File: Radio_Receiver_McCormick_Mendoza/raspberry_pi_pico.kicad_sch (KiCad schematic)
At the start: 9 parts, among them J27 Conn_01x20_Socket, J28 Conn_01x01_Pin, J29 Conn_01x20_Socket, U4 Pico

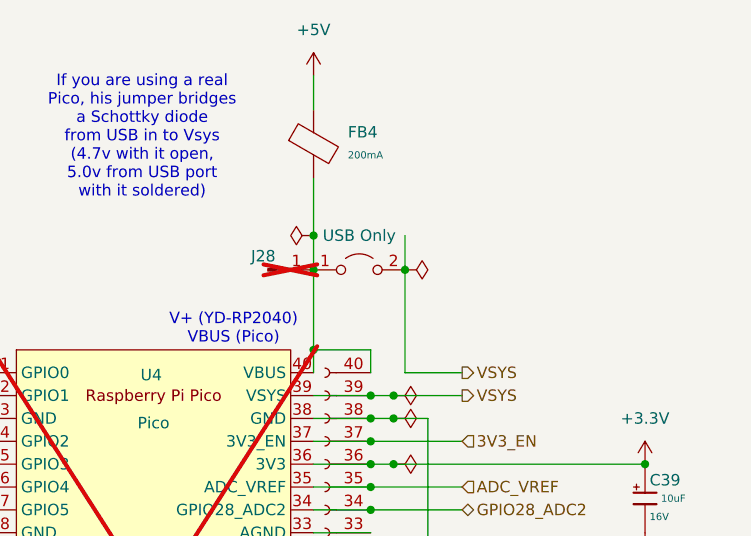
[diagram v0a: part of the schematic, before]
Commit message: Added bibliography source and schematic edits
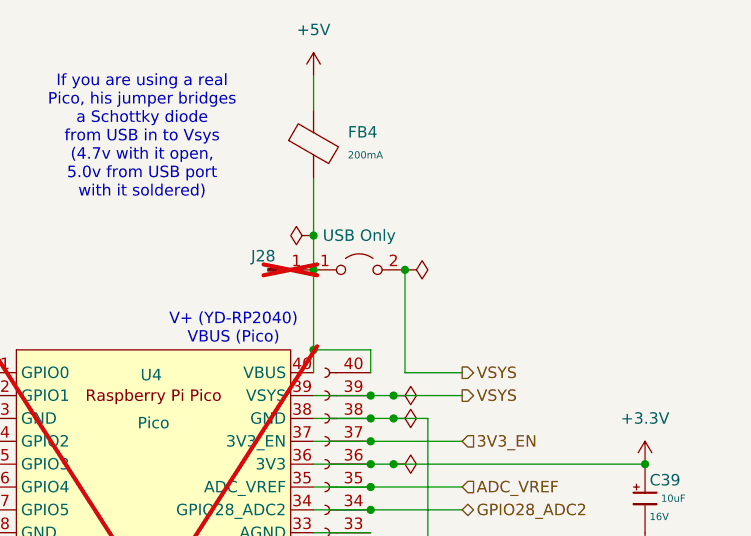
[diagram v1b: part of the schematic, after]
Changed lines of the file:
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@@
-	(wire
-		(pts
-			(xy 167.64 48.26) (xy 167.64 52.07)
-		)
-		(stroke
-			(width 0)
-			(type default)
-		)
-	)
 	(wire
 		(pts
@@
 		(length 2.54)
 		(shape round)
-		(at 172.72 73.66 90)
+		(at 189.23 73.66 180)
 		(fields_autoplaced yes)
 		(effects
@@
 				(size 1.27 1.27)
 			)
-			(justify left bottom)
+			(justify right bottom)
 		)
 		(property "Net Class" "1V1"
-			(at 170.18 72.9615 90)
+			(at 189.9285 76.2 0)
 			(hide yes)
 			(show_name no)
@@
 		)
 		(property "Component Class" ""
-			(at -41.91 5.08 0)
+			(at -25.4 5.08 0)
 			(hide yes)
 			(show_name no)

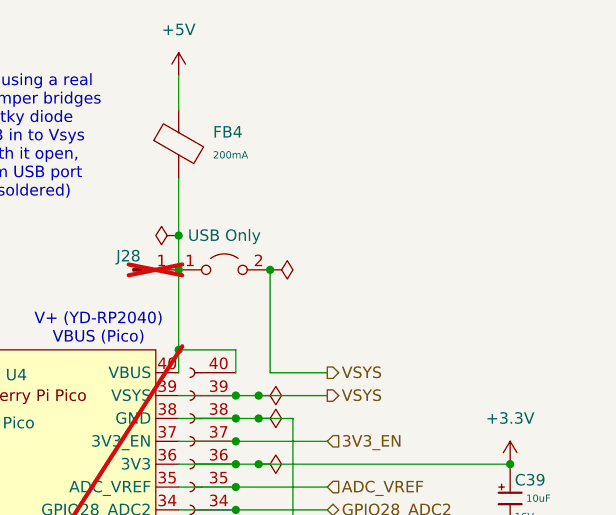
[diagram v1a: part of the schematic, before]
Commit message: Added reference voltage stability by buffer amp
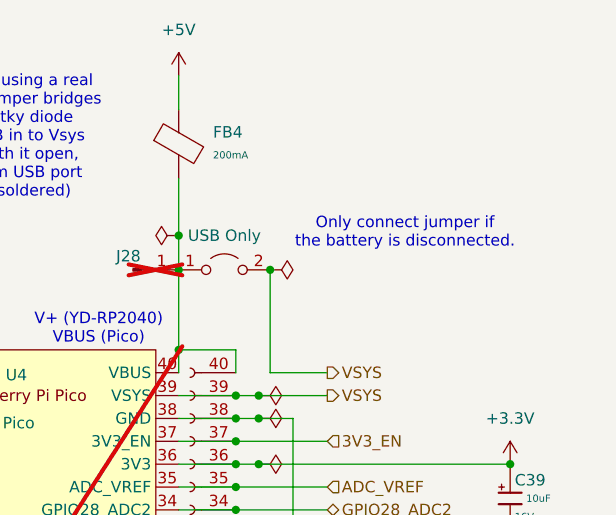
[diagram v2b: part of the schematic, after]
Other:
- note added: "Only connect jumper if the battery is disconnected."
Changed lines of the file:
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@@
 		(comment 3 "Jeffrey McCormick")
+	)
+	(text "Only connect jumper if\nthe battery is disconnected."
+		(exclude_from_sim no)
+		(at 182.626 48.006 0)
+		(effects
+			(font
+				(size 1.27 1.27)
+			)
+		)
 	)
 	(text "V+ (YD-RP2040)\nVBUS (Pico)"

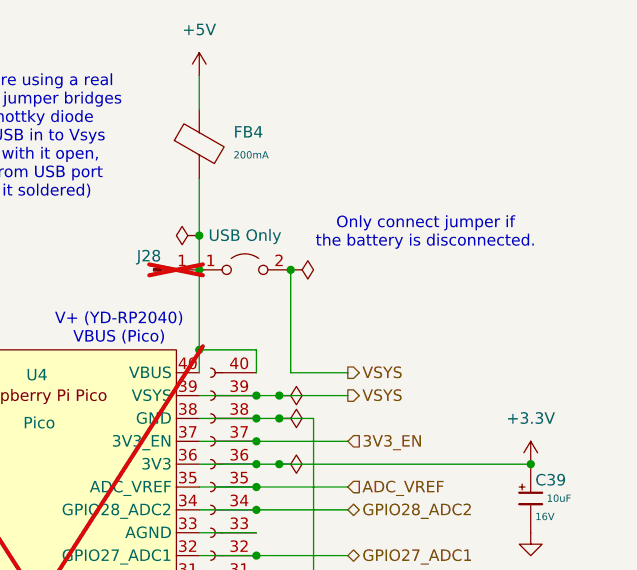
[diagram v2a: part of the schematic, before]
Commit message: Added digital power regulator
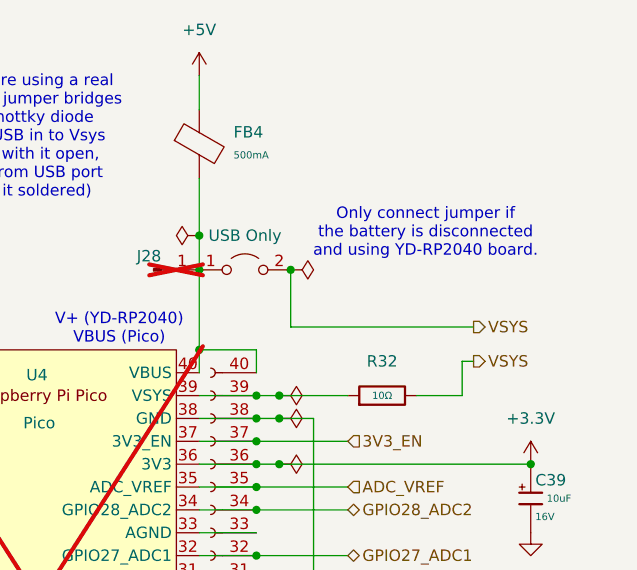
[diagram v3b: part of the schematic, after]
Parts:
- removed FB4: (no value), PCM_JLCPCB:FB_0603, symbol PCM_JLCPCB-Inductors:Ferrite,0603
- added FB4: (no value), PCM_JLCPCB:FB_0805, symbol PCM_JLCPCB-Inductors:Ferrite,0805,(2)
- added R32: 10Ω, PCM_JLCPCB:R_0805, symbol PCM_JLCPCB-Resistors:0805,10Ω
- C39: Manufacturer AVX -> (none)
- R30: Manufacturer UNI-ROYAL(Uniroyal Elec) -> (none)
- S2: Manufacturer XUNPU -> (none)
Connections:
- net +5V: now also FB4.1
- net VSYS: now also R32.2; no longer J29.39 (Pin_2), U4.39 (VSYS)
- net at J28.1 (Pin_1), J29.40 (Pin_1), JP69.1 (A)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: now also FB4.2
- new net: J29.39 (Pin_2), R32.1, U4.39 (VSYS)
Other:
- note added: "Only connect jumper if the battery is disconnected and using YD-RP2040 board."
- note removed: "Only connect jumper if the battery is disconnected."

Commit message: Integrated signal path modules
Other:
- note added: "To Digital parts (OLED, DAC, etc.)"
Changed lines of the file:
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@@
+		)
+	)
+	(text "To Digital parts\n(OLED, DAC, etc.)"
+		(exclude_from_sim no)
+		(at 205.74 71.374 0)
+		(effects
+			(font
+				(size 1.27 1.27)
+			)
 		)
 	)

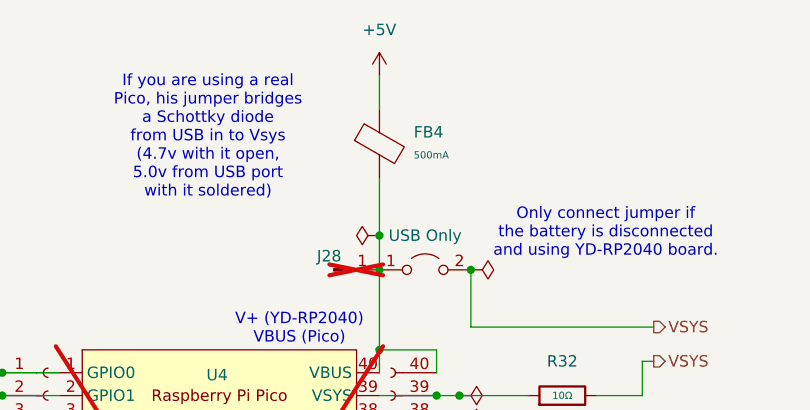
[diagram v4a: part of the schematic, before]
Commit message: Finalized Pico connections and added indicator LEDs
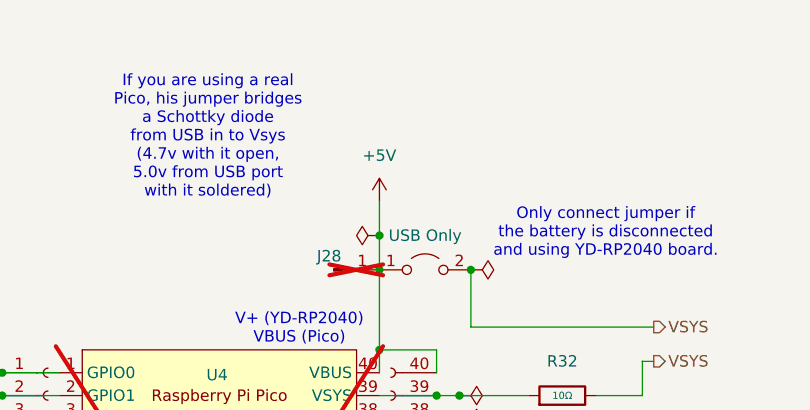
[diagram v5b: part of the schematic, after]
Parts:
- removed FB4: (no value), PCM_JLCPCB:FB_0805, symbol PCM_JLCPCB-Inductors:Ferrite,0805,(2)
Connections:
- net +5V: now also J28.1 (Pin_1), J29.40 (Pin_1), JP69.1 (A), U4.40 (VBUS)

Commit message: Added transformer footprint and datasheet
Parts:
- R32: Manufacturer UNI-ROYAL(Uniroyal Elec) -> (none)
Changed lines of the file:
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@@
-			)
-		)
-		(property "Manufacturer" "UNI-ROYAL(Uniroyal Elec)"
-			(at 177.8 66.04 0)
-			(hide yes)
-			(show_name no)
-			(do_not_autoplace no)
-			(effects
-				(font
-					(size 1.27 1.27)
-				)
 			)
 		)

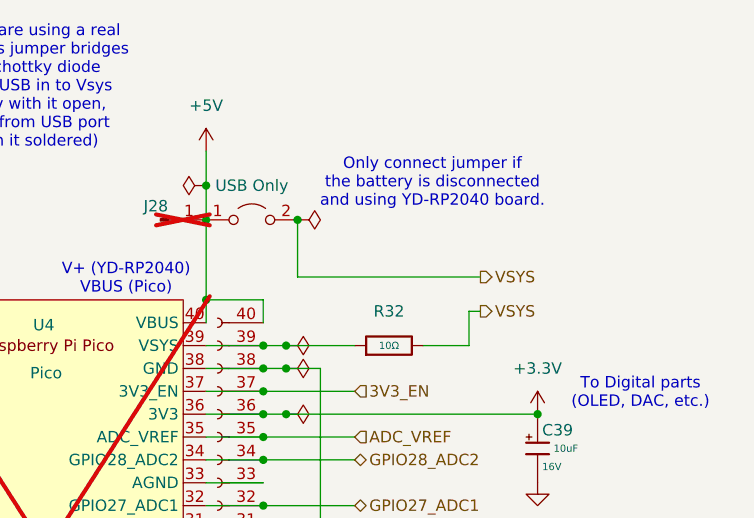
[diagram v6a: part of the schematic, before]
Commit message: Swapped voltage regulator to output 4.5V
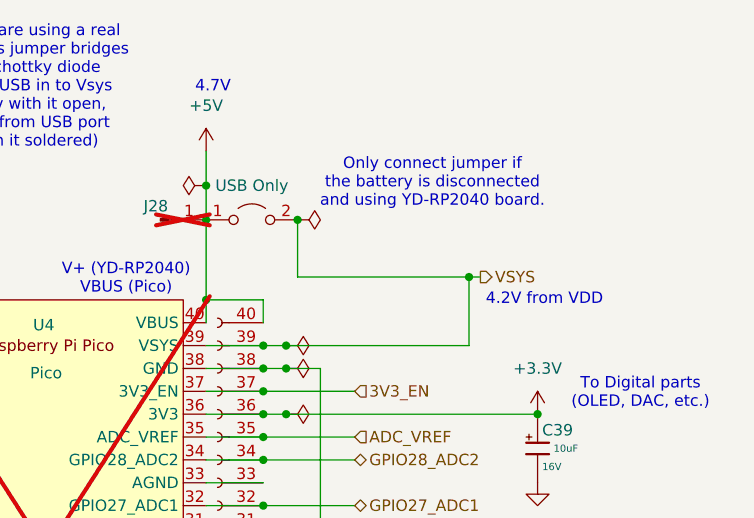
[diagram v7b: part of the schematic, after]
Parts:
- removed R32: 10Ω, PCM_JLCPCB:R_0805, symbol PCM_JLCPCB-Resistors:0805,10Ω
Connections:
- net VSYS: now also J29.39 (Pin_2), U4.39 (VSYS)
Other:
- note added: "4.2V from VDD"
- note added: "4.7V"

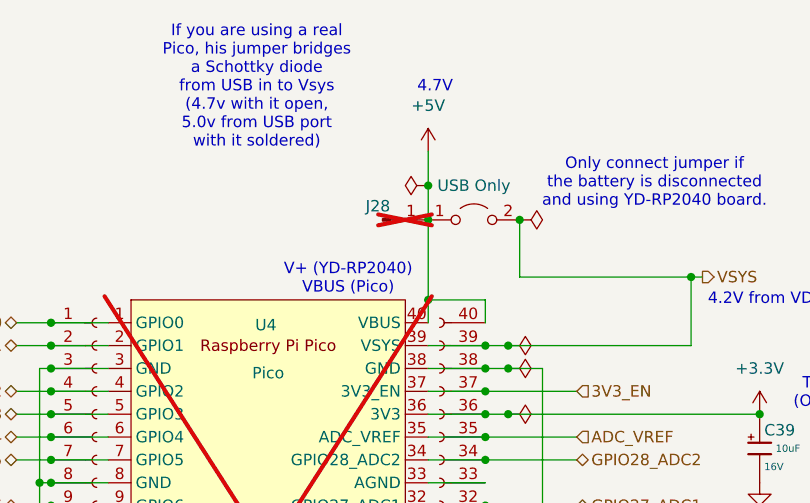
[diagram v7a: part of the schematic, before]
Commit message: Added MicroSD card and verified footprints
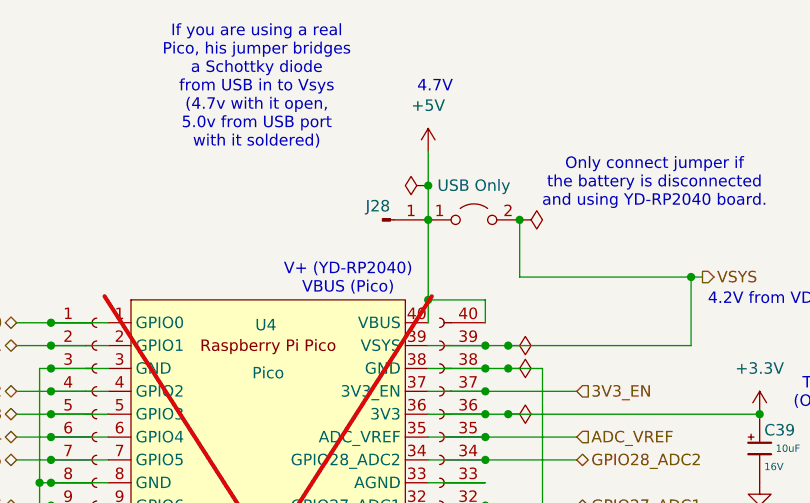
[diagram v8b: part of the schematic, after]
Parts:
- J28: now fitted
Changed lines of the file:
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@@
 		(on_board yes)
 		(in_pos_files yes)
-		(dnp yes)
+		(dnp no)
 		(property "Reference" "J28"
 			(at 151.892 50.546 0)
